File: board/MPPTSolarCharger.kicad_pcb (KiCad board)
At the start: 2 copper layers, 150.5 x 49.5 mm, 49 parts, among them J1 Screw_Terminal_01x02, J2 Screw_Terminal_01x02, J3 Conn_01x06, Q1 PSMN5R5-60YS, Q2 PSMN5R5-60YS, Q3 PSMN5R5-60YS, U1 LM350_TO220, U2 MIC4605-1YM, U3 INA260, U4 INA260

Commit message: Rev 2 of board layout, WIP
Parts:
- removed C11: 1000uF, Capacitor_THT:CP_Radial_D16.0mm_P7.50mm
- removed JP2, JP4: Jumper_NC_Small, Connector_PinHeader_2.54mm:PinHeader_1x02_P2.54mm_Vertical
- removed R5: 3.3, Resistor_SMD:R_0805_2012Metric
- C1, C12, C13, C14, C15, C16, C17, C2, C8, C9: footprint Capacitor_SMD:C_0805_2012Metric -> Capacitor_SMD:C_0805_2012Metric_Pad1.15x1.40mm_HandSolder
- C5, C7: footprint Capacitor_SMD:C_0805_2012Metric -> Capacitor_SMD:C_1210_3225Metric_Pad1.42x2.65mm_HandSolder
- D1, D2: footprint Diode_THT:D_DO-35_SOD27_P7.62mm_Horizontal -> Diode_SMD:D_SOD-323_HandSoldering
- J1, J2: footprint TerminalBlock_Phoenix:TerminalBlock_Phoenix_MKDS-3-2-5.08_1x02_P5.08mm_Horizontal -> Saintgimp:Phoenix_Contact_MKDS_5-2-952
- R1, R2, R3, R4, R7, R8, R9: footprint Resistor_SMD:R_0805_2012Metric -> Resistor_SMD:R_0805_2012Metric_Pad1.15x1.40mm_HandSolder
- R6: footprint Resistor_SMD:R_0805_2012Metric -> Resistor_SMD:R_1206_3216Metric_Pad1.42x1.75mm_HandSolder
- moved F1 109.0 mm to (124.5, 143.5), turned to 90 degrees
- moved C13 106.5 mm to (118.9, 146.3)
- moved J2 92.6 mm to (138.4, 141.0), turned to 0 degrees
- moved R8 76.7 mm to (98.6, 95.9), turned to 180 degrees
- moved R9 74.9 mm to (98.6, 93.3), turned to 180 degrees
- moved J3 74.9 mm to (94.1, 83.2), turned to 0 degrees
- moved C17 72.8 mm to (137.9, 125.0), turned to 90 degrees
- moved C16 69.7 mm to (146.1, 131.8)
- moved TP6 67.0 mm to (137.9, 117.6)
- moved U4 63.2 mm to (143.0, 125.0), turned to 270 degrees
- moved C10 54.2 mm to (142.2, 110.5), turned to 0 degrees
- moved J1 50.9 mm to (100.3, 141.0), turned to 0 degrees
- moved TP4 48.8 mm to (105.4, 94.0)
- moved C3 40.7 mm to (100.3, 125.7), turned to 180 degrees
- moved C1 40.4 mm to (105.4, 133.3), turned to 0 degrees
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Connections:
- C4 pad 1: Net-(C4-Pad1) -> /PowerStage/SOLAR+
- C9 pad 1: /PowerStage/SWITCH_NODE -> /PowerStage/HB
- C9 pad 2: /PowerStage/HB -> /PowerStage/SWITCH_NODE
- D1 pad 2: Net-(D1-Pad2) -> /PowerStage/LOW_DRIVER
- Q3 pad 4: Net-(D1-Pad2) -> /PowerStage/LOW_DRIVER
- TP2 pad 1: Net-(D1-Pad2) -> /PowerStage/LOW_DRIVER
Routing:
- net /PowerStage/SOLAR+: track 11.9 -> 71.3 mm, vias 0 -> 2
- net /PowerStage/BUCK_OUT: track 103.0 -> 45.6 mm
- net Net-(D1-Pad2): track 43.1 -> 0.00 mm, vias 2 -> 0
- net /PowerStage/SWITCH_NODE: track 2.54 -> 36.1 mm
- net GND: track 26.1 -> 0.00 mm, vias 60 -> 9
- net /PowerStage/LOW_DRIVER: track 3.04 -> 28.3 mm
- net /MCU/HIGH_PWM: track 46.0 -> 29.4 mm
- net /MCU/LOW_PWM: track 46.9 -> 30.5 mm
- net /MCU/SDA: track 119.3 -> 135.1 mm
- net Net-(C4-Pad1): track 14.0 -> 0.00 mm
- net /MCU/SCL: track 124.4 -> 138.0 mm
- net +10V: track 43.9 -> 32.5 mm
- net +3V3: track 159.8 -> 171.0 mm, vias 6 -> 2
- net Net-(C11-Pad1): track 7.62 -> 0.00 mm
- net /PowerStage/HIGH_DRIVER: track 18.7 -> 11.3 mm, vias 2 -> 0
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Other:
- board outline removed
- board text added: "Saint Gimp MPPT Solar Charger Prototype v0.2"
- board text removed: "Saint Gimp MPPT Solar Charger Prototype v0.1"

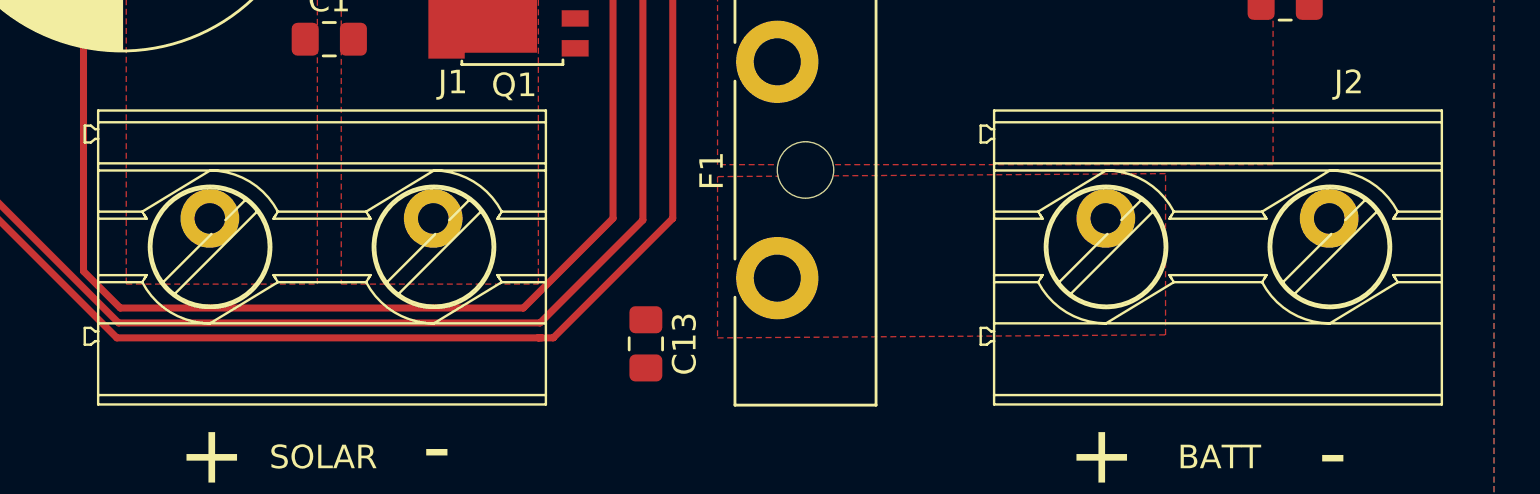
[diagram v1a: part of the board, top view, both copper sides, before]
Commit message: Upgrade to KiCad 6
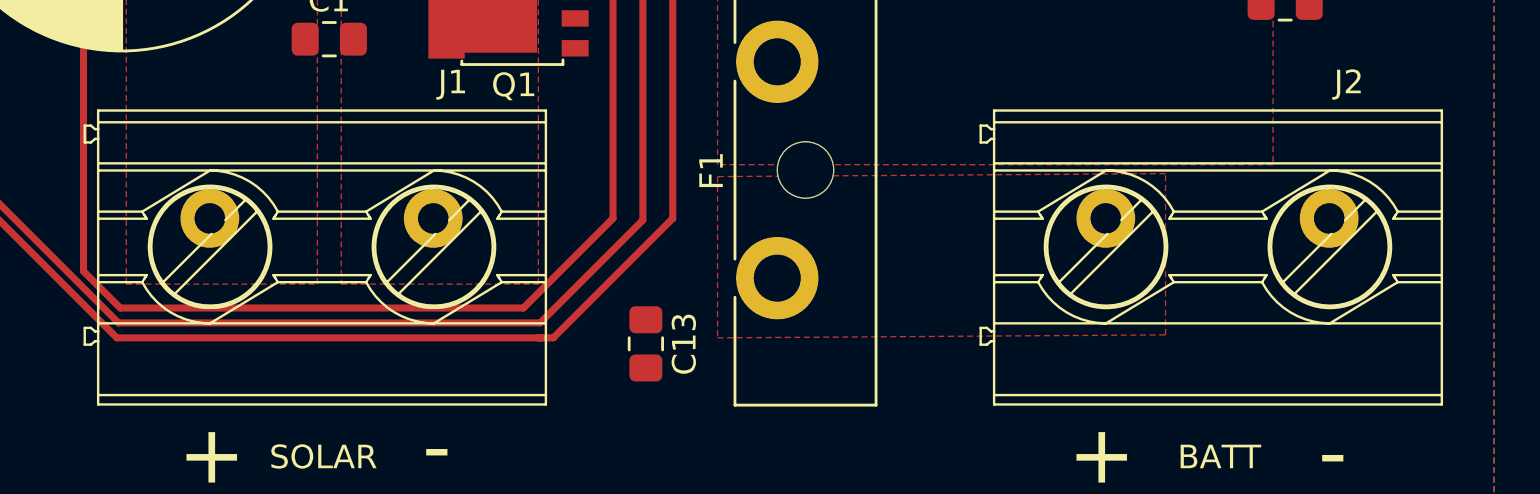
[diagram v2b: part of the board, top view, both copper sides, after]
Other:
- net class Default removed

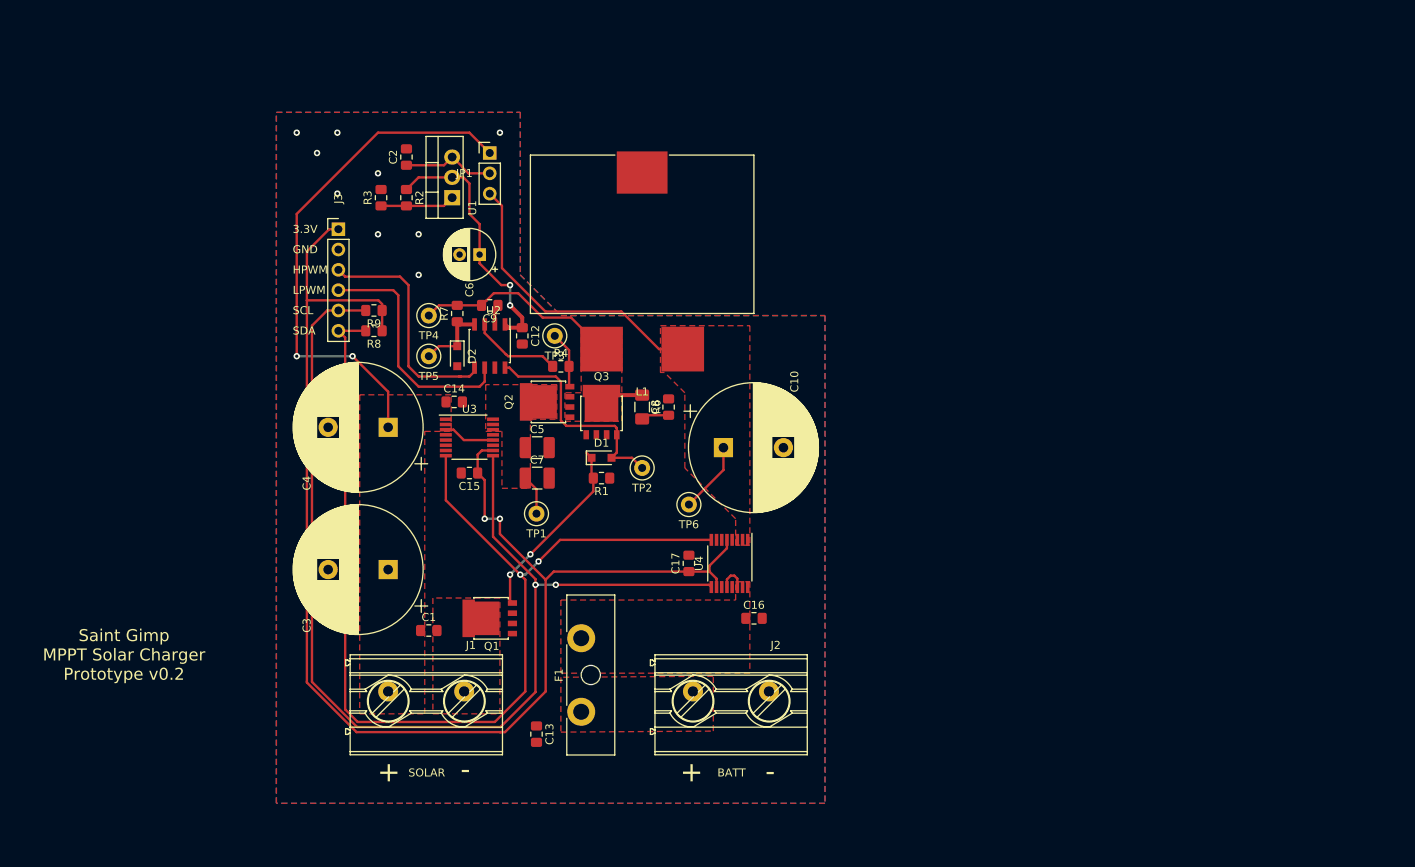
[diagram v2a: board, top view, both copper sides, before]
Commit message: Different board layout, WIP
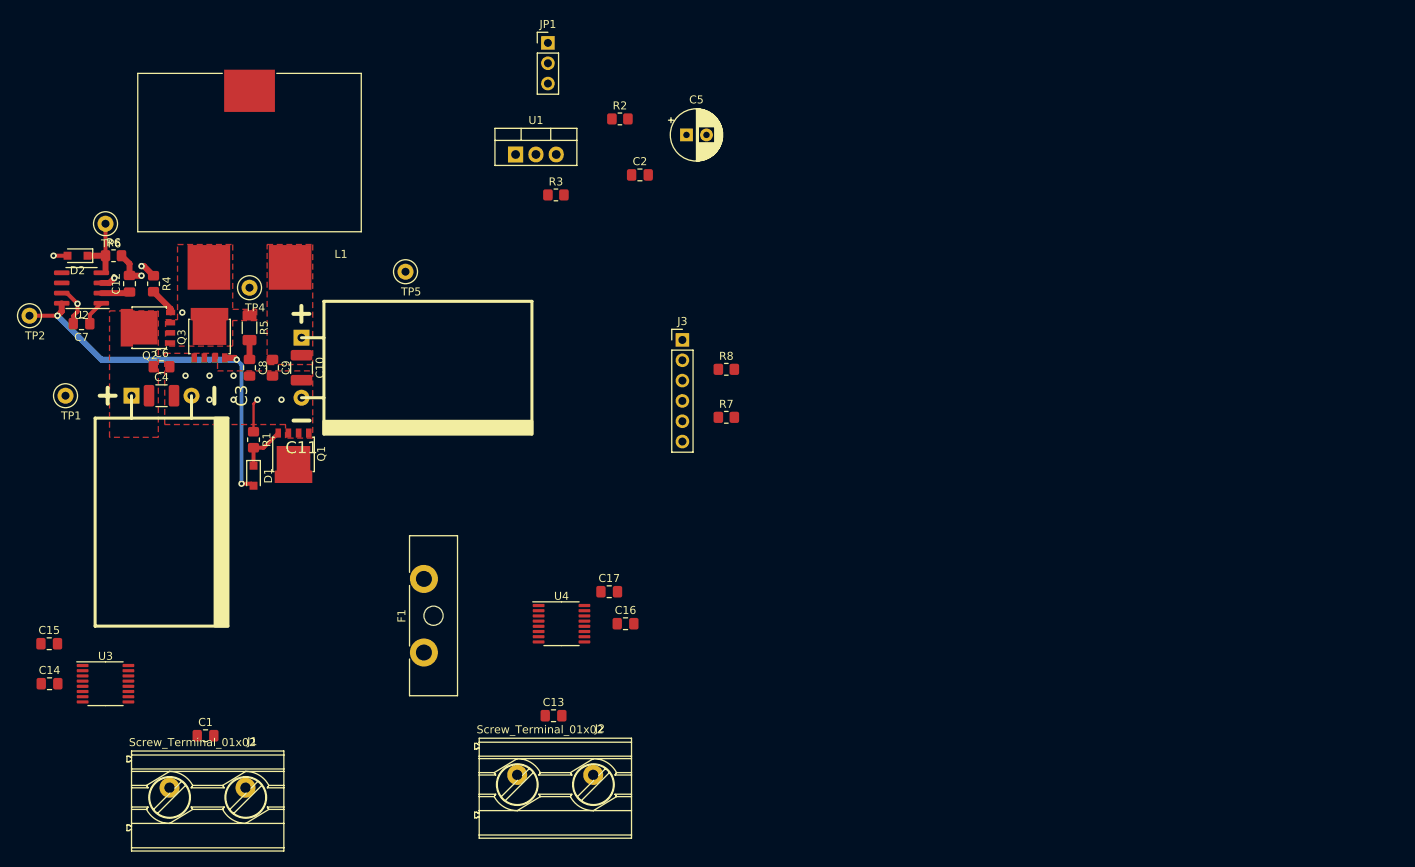
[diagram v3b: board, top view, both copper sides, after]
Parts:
- removed R9: 4.3K, Resistor_SMD:R_0805_2012Metric_Pad1.15x1.40mm_HandSolder
- removed TP3: TestPoint_Probe, TestPoint:TestPoint_Loop_D2.50mm_Drill1.0mm
- added C11: 1000uF, SaintGimp:CP_16x25mm_horiz-L, F.Cu at (89.5, 100.5)
- added R5: 2.2, Resistor_SMD:R_1206_3216Metric_Pad1.30x1.75mm_HandSolder, F.Cu at (83.0, 95.5)
- C1, C12, C13, C14, C15, C16, C17, C2, C8: footprint Capacitor_SMD:C_0805_2012Metric_Pad1.15x1.40mm_HandSolder -> Capacitor_SMD:C_0805_2012Metric_Pad1.18x1.45mm_HandSolder
- C10, C4: value 1000uF -> 4.7uF; footprint Capacitor_THT:CP_Radial_D16.0mm_P7.50mm -> Capacitor_SMD:C_1210_3225Metric_Pad1.33x2.70mm_HandSolder
- C3: footprint Capacitor_THT:CP_Radial_D16.0mm_P7.50mm -> SaintGimp:CP_16x25mm_horiz-R
- C5: value 4.7uF -> 100uF; footprint Capacitor_SMD:C_1210_3225Metric_Pad1.42x2.65mm_HandSolder -> Capacitor_THT:CP_Radial_D6.3mm_P2.50mm
- C6: value 100uF -> 10nF; footprint Capacitor_THT:CP_Radial_D6.3mm_P2.50mm -> Capacitor_SMD:C_0805_2012Metric_Pad1.18x1.45mm_HandSolder
- C7: value 4.7uF -> 1uF; footprint Capacitor_SMD:C_1210_3225Metric_Pad1.42x2.65mm_HandSolder -> Capacitor_SMD:C_0805_2012Metric_Pad1.18x1.45mm_HandSolder
- C9: value 1uF -> 10nF; footprint Capacitor_SMD:C_0805_2012Metric_Pad1.15x1.40mm_HandSolder -> Capacitor_SMD:C_0805_2012Metric_Pad1.18x1.45mm_HandSolder
- J1, J2: footprint Saintgimp:Phoenix_Contact_MKDS_5-2-952 -> SaintGimp:Phoenix_Contact_MKDS_5-2-952
- L1: footprint Saintgimp:Coilcraft_SER2900 -> SaintGimp:Coilcraft_SER2900
- R1, R2, R3, R4, R8: footprint Resistor_SMD:R_0805_2012Metric_Pad1.15x1.40mm_HandSolder -> Resistor_SMD:R_0805_2012Metric_Pad1.20x1.40mm_HandSolder
- R6: value 2.2 -> 3.3; footprint Resistor_SMD:R_1206_3216Metric_Pad1.42x1.75mm_HandSolder -> Resistor_SMD:R_0805_2012Metric_Pad1.20x1.40mm_HandSolder
- R7: value 3 -> 4.3K; footprint Resistor_SMD:R_0805_2012Metric_Pad1.15x1.40mm_HandSolder -> Resistor_SMD:R_0805_2012Metric_Pad1.20x1.40mm_HandSolder
- moved TP6 80.9 mm to (65.0, 82.5)
- moved TP2 78.9 mm to (55.5, 94.0)
- moved R6 68.7 mm to (66.0, 86.5), turned to 0 degrees
- moved C14 61.6 mm to (58.0, 140.0)
- moved TP1 60.7 mm to (60.0, 104.0)
- moved C7 60.1 mm to (62.0, 95.0), turned to 180 degrees
- moved C15 56.7 mm to (58.0, 135.0), turned to 0 degrees
- moved U3 54.9 mm to (65.0, 140.0)
- moved C10 53.7 mm to (89.5, 100.5), turned to -90 degrees
- moved C8 52.6 mm to (83.0, 100.5), turned to -90 degrees
- moved R4 52.0 mm to (71.0, 90.0), turned to -90 degrees
- moved U2 51.5 mm to (62.0, 90.5), turned to 180 degrees
- moved Q2 50.8 mm to (70.3, 95.5)
- moved L1 50.1 mm to (83.0, 73.6)
- moved Q3 49.9 mm to (78.0, 96.4)
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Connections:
- C12 pad 1: +10V -> /PowerStage/HB
- C12 pad 2: GND -> /PowerStage/SWITCH_NODE
- C15 pad 1: +3V3 -> +3.3V
- C17 pad 1: +3V3 -> +3.3V
- C3 pad 1: /PowerStage/SOLAR+ -> /PowerStage/BUCK_IN
- C4 pad 1: /PowerStage/SOLAR+ -> /PowerStage/BUCK_IN
- C5 pad 1: /PowerStage/SolarCurrentMonitor/IN- -> +10V
- C6 pad 1: +10V -> /PowerStage/BUCK_IN
- C7 pad 1: /PowerStage/SolarCurrentMonitor/IN- -> +10V
- C9 pad 1: /PowerStage/HB -> /PowerStage/BUCK_OUT
- C9 pad 2: /PowerStage/SWITCH_NODE -> GND
- J3 pad 1: +3V3 -> +3.3V
- JP1 pad 2: Net-(C2-Pad1) -> unconnected-(JP1-Pad2)
- Q2 pad 5: /PowerStage/SolarCurrentMonitor/IN- -> /PowerStage/BUCK_IN
- R6 pad 1: /PowerStage/SWITCH_NODE -> /PowerStage/HS
- R6 pad 2: Net-(C8-Pad1) -> /PowerStage/SWITCH_NODE
- R7 pad 1: /PowerStage/HS -> +3.3V
- R7 pad 2: /PowerStage/SWITCH_NODE -> /MCU/SDA
- R8 pad 1: +3V3 -> +3.3V
- R8 pad 2: /MCU/SDA -> /MCU/SCL
- TP1 pad 1: /PowerStage/SolarCurrentMonitor/IN- -> /PowerStage/BUCK_IN
- TP5 pad 1: /PowerStage/HS -> /PowerStage/BUCK_OUT
- TP6 pad 1: /PowerStage/BUCK_OUT -> /PowerStage/HS
- U3 pad 10: +3V3 -> +3.3V
- U3 pad 13: Net-(U3-Pad13) -> unconnected-(U3-Pad13)
- U3 pad 14: /PowerStage/SolarCurrentMonitor/IN- -> /PowerStage/BUCK_IN
- U3 pad 15: /PowerStage/SolarCurrentMonitor/IN- -> /PowerStage/BUCK_IN
- U3 pad 16: /PowerStage/SolarCurrentMonitor/IN- -> /PowerStage/BUCK_IN
- U3 pad 7: Net-(U3-Pad7) -> unconnected-(U3-Pad7)
- U4 pad 10: +3V3 -> +3.3V
- U4 pad 13: Net-(U4-Pad13) -> unconnected-(U4-Pad13)
- U4 pad 5: +3V3 -> +3.3V
- U4 pad 7: Net-(U4-Pad7) -> unconnected-(U4-Pad7)
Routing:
- net +3V3: track 171.0 -> 0.00 mm, vias 2 -> 0
- net /MCU/SCL: track 138.0 -> 0.00 mm, vias 2 -> 0
- net /MCU/SDA: track 135.1 -> 0.00 mm, vias 2 -> 0
- net /PowerStage/SOLAR+: track 71.3 -> 0.00 mm, vias 2 -> 0
- net /PowerStage/BUCK_OUT: track 45.6 -> 0.00 mm
- net /MCU/LOW_PWM: track 30.5 -> 0.00 mm
- net /MCU/HIGH_PWM: track 29.4 -> 0.00 mm
- net +10V: track 32.5 -> 3.15 mm, vias 2 -> 0
- net /PowerStage/SWITCH_NODE: track 36.1 -> 12.6 mm, vias 0 -> 2
- net /PowerStage/LOW_DRIVER: track 28.3 -> 48.9 mm, vias 0 -> 3
- net Net-(D1-Pad1): track 23.6 -> 6.10 mm, vias 2 -> 0
- net Net-(C2-Pad1): track 11.7 -> 0.00 mm
- net GND: track 0.00 -> 11.2 mm
- net Net-(R2-Pad2): track 9.31 -> 0.00 mm
- net /PowerStage/SolarCurrentMonitor/IN-: track 7.37 -> 0.00 mm
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- added copper zone on F.Cu, net /PowerStage/BUCK_IN
- added copper zone on In1.Cu, net GND
- added copper zone on In2.Cu, net GND
- removed copper zone on F.Cu, net /PowerStage/BATTERY+
- removed copper zone on F.Cu, net /PowerStage/BatteryCurrentMonitor/IN-
- removed copper zone on F.Cu, net /PowerStage/SOLAR+
- removed copper zone on F.Cu, net /PowerStage/SOLAR-
- removed copper zone on F.Cu, net /PowerStage/SolarCurrentMonitor/IN-
- removed copper zone on B.Cu, net GND
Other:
- copper layers 2 -> 4
- rule pad_to_mask_clearance: 0.2 -> 0
- board text removed: "+"
- board text removed: "-"
- board text removed: "3.3V"
- board text removed: "BATT"
- board text removed: "GND"
- board text removed: "HPWM"
- board text removed: "LPWM"
- board text removed: "SCL"
- board text removed: "SDA"
- board text removed: "SOLAR"
- board text removed: "Saint Gimp MPPT Solar Charger Prototype v0.2"
